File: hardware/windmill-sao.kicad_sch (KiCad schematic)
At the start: 27 parts, among them J1 SAO, J2 QWIIC, M1 SG90, U1 CH32V003F4P6

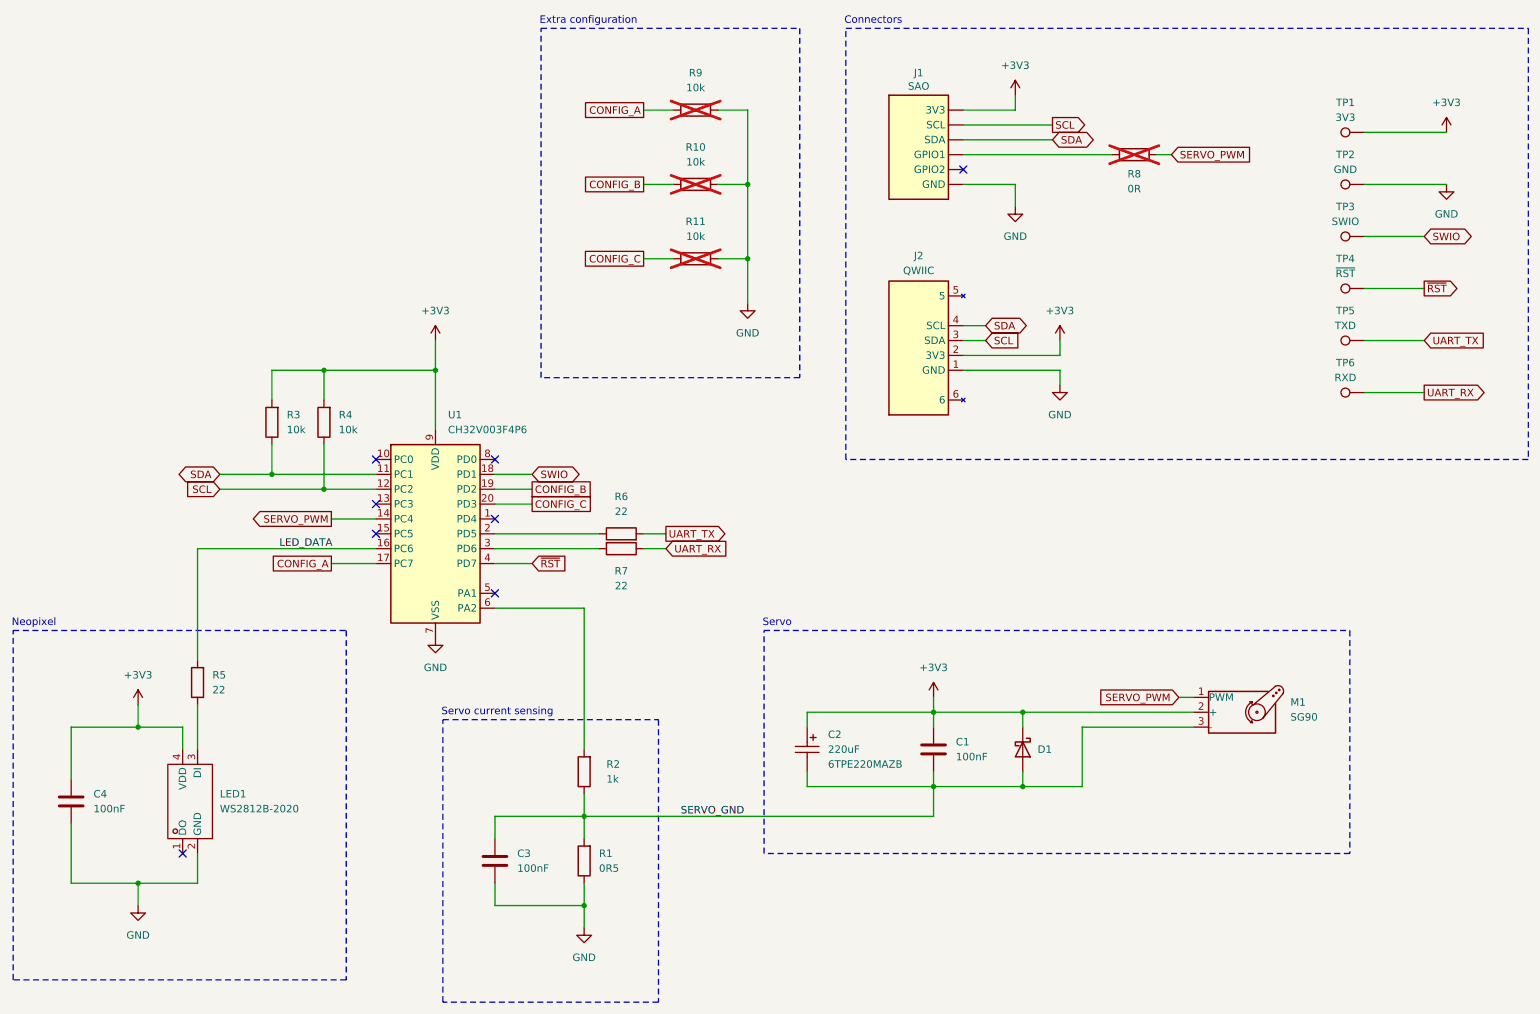
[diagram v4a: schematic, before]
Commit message: Add QWIIC logo and supplier part numbers
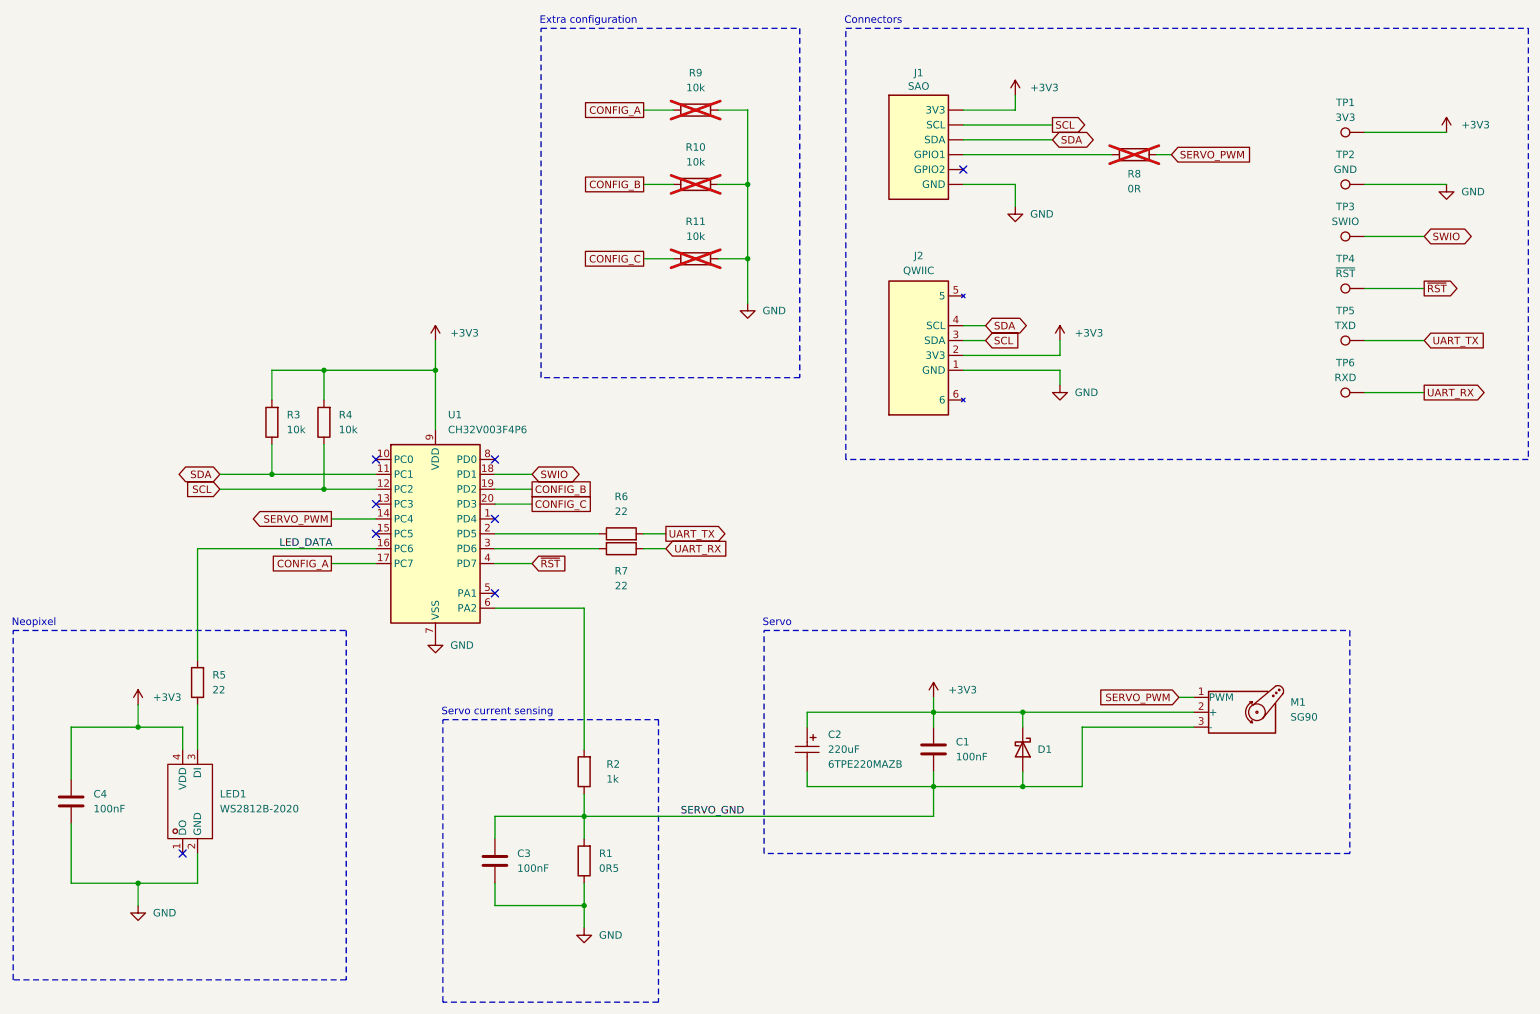
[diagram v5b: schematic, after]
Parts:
- C1, C3, C4: LCSC Part # (none) -> C14663
- C2: LCSC Part # (none) -> C79111; Supplier Part C79111 -> (none)
- D1: LCSC Part # (none) -> C2480
- J2: LCSC Part # (none) -> C160404; Supplier Part C160404 -> (none)
- LED1: JLCPCB Part # (none) -> C965555; LCSC Part # (none) -> C965555; Supplier Part C965555 -> (none)
- R1: LCSC Part # (none) -> C25340
- R2: LCSC Part # (none) -> C21190
- R3, R4: LCSC Part # (none) -> C25804
- R5, R6, R7: LCSC Part # (none) -> C23345
- U1: LCSC Part # (none) -> C5187096; Supplier Part C5187096 -> (none)
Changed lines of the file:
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@@
 			)
 		)
+		(property "LCSC Part #" "C21190"
+			(at 115.57 147.32 0)
+			(hide yes)
+			(show_name no)
+			(do_not_autoplace no)
+			(effects
+				(font
+					(size 1.27 1.27)
+				)
+			)
+		)
 		(pin "2"
 		)
@@
 		)
 		(property "Value" "+3V3"
-			(at 90.17 68.58 0)
+			(at 92.71 72.3899 0)
 			(show_name no)
 			(do_not_autoplace no)
@@
 					(size 1.27 1.27)
 				)
+				(justify left)
 			)
 		)
@@
 		(in_bom no)
 		(on_board yes)
-		(in_pos_files yes)
+		(in_pos_files no)
 		(dnp no)
 		(fields_autoplaced yes)
@@
 			)
 		)
-		(property "Supplier Part" "C79111"
+		(property "Supplier" "LCSC"
 			(at 153.67 143.51 0)
 			(hide yes)
@@
 			)
 		)
-		(property "Supplier" "LCSC"
+		(property "LCSC Part Name" "220uF ±20% 6.3V MSL=3拆包后请尽快使用"
 			(at 153.67 143.51 0)
 			(hide yes)
@@
 			)
 		)
-		(property "LCSC Part Name" "220uF ±20% 6.3V MSL=3拆包后请尽快使用"
+		(property "LCSC Part #" "C79111"
 			(at 153.67 143.51 0)
 			(hide yes)
@@
 		(in_bom no)
 		(on_board yes)
-		(in_pos_files yes)
+		(in_pos_files no)
 		(dnp no)
 		(fields_autoplaced yes)
@@
 		(in_bom no)
 		(on_board yes)
-		(in_pos_files yes)
+		(in_pos_files no)
 		(dnp no)
 		(fields_autoplaced yes)
@@
 			)
 		)
+		(property "LCSC Part #" "C23345"
+			(at 121.92 106.68 90)
+			(hide yes)
+			(show_name no)
+			(do_not_autoplace no)
+			(effects
+				(font
+					(size 1.27 1.27)
+				)
+			)
+		)
 		(pin "2"
 		)
@@
 		)
 		(property "Value" "GND"
-			(at 115.57 179.07 0)
+			(at 118.11 175.2599 0)
 			(show_name no)
 			(do_not_autoplace no)
@@
 					(size 1.27 1.27)
 				)
+				(justify left)
 			)
 		)
@@
 		)
 		(property "Value" "GND"
-			(at 189.23 55.88 0)
+			(at 191.77 52.0699 0)
 			(show_name no)
 			(do_not_autoplace no)
@@
 					(size 1.27 1.27)
 				)
+				(justify left)
 			)
 		)
@@
 		)
 		(property "Value" "GND"
-			(at 196.85 86.36 0)
+			(at 199.39 82.5499 0)
 			(show_name no)
 			(do_not_autoplace no)
@@
 					(size 1.27 1.27)
 				)
+				(justify left)
 			)
 		)
@@
 			)
 		)
+		(property "LCSC Part #" "C14663"
+			(at 175.26 143.51 0)
+			(hide yes)
+			(show_name no)
+			(do_not_autoplace no)
+			(effects
+				(font
+					(size 1.27 1.27)
+				)
+			)
+		)
 		(pin "1"
 		)
@@
 		)
 		(property "Value" "+3V3"
-			(at 196.85 68.58 0)
+			(at 199.39 72.3899 0)
 			(show_name no)
 			(do_not_autoplace no)
@@
 					(size 1.27 1.27)
 				)
+				(justify left)
 			)
 		)
@@
 			)
 		)
-		(property "Supplier Part" "C5187096"
+		(property "LCSC Part #" "C5187096"
 			(at 90.17 106.68 0)
 			(hide yes)
@@
 		)
 		(property "Value" "+3V3"
-			(at 262.89 33.02 0)
+			(at 265.43 36.8299 0)
 			(show_name no)
 			(do_not_autoplace no)
@@
 					(size 1.27 1.27)
 				)
+				(justify left)
 			)
 		)
@@
 			)
 		)
+		(property "LCSC Part #" "C25340"
+			(at 115.57 162.56 0)
+			(hide yes)
+			(show_name no)
+			(do_not_autoplace no)
+			(effects
+				(font
+					(size 1.27 1.27)
+				)
+			)
+		)
 		(pin "2"
 		)
@@
 		(in_bom no)
 		(on_board yes)
-		(in_pos_files yes)
+		(in_pos_files no)
 		(dnp no)
 		(fields_autoplaced yes)
@@
 			)
 		)
+		(property "LCSC Part #" "C14663"
+			(at 100.33 162.56 0)
+			(hide yes)
+			(show_name no)
+			(do_not_autoplace no)
+			(effects
+				(font
+					(size 1.27 1.27)
+				)
+			)
+		)
 		(pin "1"
 		)
@@
 		)
 		(property "Value" "+3V3"
-			(at 189.23 26.67 0)
+			(at 191.77 30.4799 0)
 			(show_name no)
 			(do_not_autoplace no)
@@
 					(size 1.27 1.27)
 				)
+				(justify left)
 			)
 		)
@@
 			)
 		)
-		(property "Supplier Part" "C965555"
+		(property "JLCPCB Part #" "C965555"
 			(at 48.26 152.4 0)
 			(hide yes)
@@
 			)
 		)
+		(property "LCSC Part #" "C965555"
+			(at 48.26 152.4 0)
+			(hide yes)
+			(show_name no)
+			(do_not_autoplace no)
+			(effects
+				(font
+					(size 1.27 1.27)
+				)
+			)
+		)
 		(pin "4"
 		)
@@
 		)
 		(property "Value" "GND"
-			(at 90.17 129.54 0)
+			(at 92.71 125.7299 0)
 			(show_name no)
 			(do_not_autoplace no)
@@
 					(size 1.27 1.27)
 				)
+				(justify left)
 			)
 		)
@@
 			)
 		)
-		(property "Supplier Part" "C160404"
+		(property "LCSC Part #" "C160404"
 			(at 176.53 74.93 90)
 			(hide yes)
@@
 		(in_bom no)
 		(on_board yes)
-		(in_pos_files yes)
+		(in_pos_files no)
 		(dnp no)
 		(fields_autoplaced yes)
@@
 		)
 		(property "Value" "GND"
-			(at 39.37 175.26 0)
+			(at 41.91 171.4499 0)
 			(show_name no)
 			(do_not_autoplace no)
@@
 					(size 1.27 1.27)
 				)
+				(justify left)
 			)
 		)
@@
 			)
 		)
+		(property "LCSC Part #" "C23345"
+			(at 49.53 132.08 0)
+			(hide yes)
+			(show_name no)
+			(do_not_autoplace no)
+			(effects
+				(font
+					(size 1.27 1.27)
+				)
+			)
+		)
 		(pin "2"
 		)
@@
 			)
 		)
+		(property "LCSC Part #" "C23345"
+			(at 121.92 109.22 90)
+			(hide yes)
+			(show_name no)
+			(do_not_autoplace no)
+			(effects
+				(font
+					(size 1.27 1.27)
+				)
+			)
+		)
 		(pin "2"
 		)
@@
 			)
 		)
+		(property "LCSC Part #" "C25804"
+			(at 62.23 87.63 0)
+			(hide yes)
+			(show_name no)
+			(do_not_autoplace no)
+			(effects
+				(font
+					(size 1.27 1.27)
+				)
+			)
+		)
 		(pin "2"
 		)
@@
 			)
 		)
+		(property "LCSC Part #" "C25804"
+			(at 71.12 87.63 0)
+			(hide yes)
+			(show_name no)
+			(do_not_autoplace no)
+			(effects
+				(font
+					(size 1.27 1.27)
+				)
+			)
+		)
 		(pin "2"
 		)
@@
 			)
 		)
+		(property "LCSC Part #" "C2480"
+			(at 190.5 143.51 90)
+			(hide yes)
+			(show_name no)
+			(do_not_autoplace no)
+			(effects
+				(font
+					(size 1.27 1.27)
+				)
+			)
+		)
 		(pin "2"
 		)
@@
 		)
 		(property "Value" "GND"
-			(at 262.89 52.07 0)
+			(at 265.43 48.2599 0)
 			(show_name no)
 			(do_not_autoplace no)
@@
 					(size 1.27 1.27)
 				)
+				(justify left)
 			)
 		)
@@
 		)
 		(property "Value" "+3V3"
-			(at 175.26 129.54 0)
+			(at 177.8 133.3499 0)
 			(show_name no)
 			(do_not_autoplace no)
@@
 					(size 1.27 1.27)
 				)
+				(justify left)
 			)
 		)
@@
 		)
 		(property "Value" "+3V3"
-			(at 39.37 130.81 0)
+			(at 41.91 134.6199 0)
 			(show_name no)
 			(do_not_autoplace no)
@@
 					(size 1.27 1.27)
 				)
+				(justify left)
 			)
 		)
@@
 			)
 		)
+		(property "LCSC Part #" "C14663"
+			(at 27.94 152.4 0)
+			(hide yes)
+			(show_name no)
+			(do_not_autoplace no)
+			(effects
+				(font
+					(size 1.27 1.27)
+				)
+			)
+		)
 		(pin "1"
 		)
@@
 		)
 		(property "Value" "GND"
-			(at 143.51 72.39 0)
+			(at 146.05 68.5799 0)
 			(show_name no)
 			(do_not_autoplace no)
@@
 					(size 1.27 1.27)
 				)
+				(justify left)
 			)
 		)
@@
 		(in_bom no)
 		(on_board yes)
-		(in_pos_files yes)
+		(in_pos_files no)
 		(dnp no)
 		(fields_autoplaced yes)

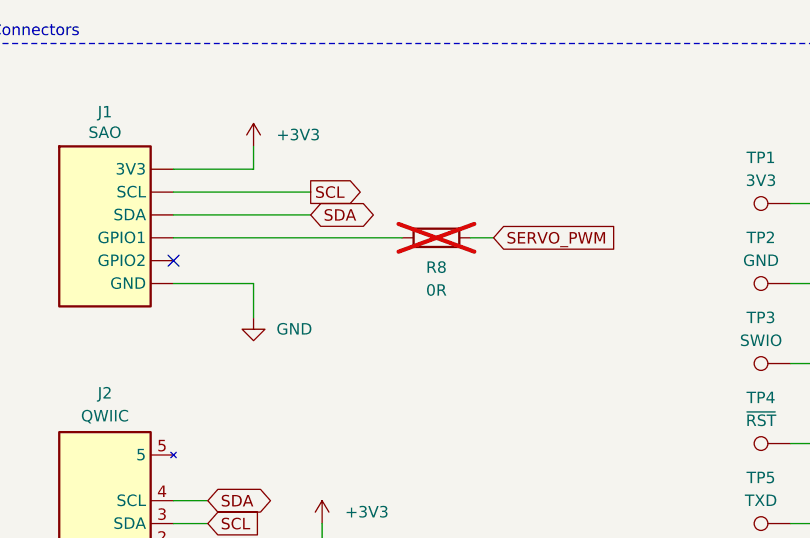
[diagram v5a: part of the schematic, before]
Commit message: Add C5 and clean up silkscreen even more
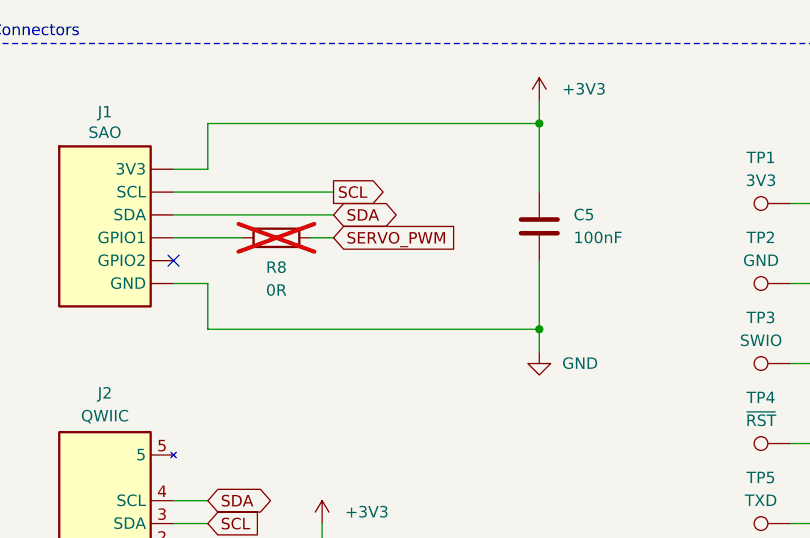
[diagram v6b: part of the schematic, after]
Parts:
- added C5: 100nF, Capacitor_SMD:C_0603_1608Metric_Pad1.08x0.95mm_HandSolder, symbol Device:C
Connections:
- net +3V3: now also C5.1
- net GND: now also C5.2
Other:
- moved on the sheet: R8
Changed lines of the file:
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@@
 	)
 	(junction
+		(at 220.98 29.21)
+		(diameter 0)
+		(color 0 0 0 0)
+	)
+	(junction
 		(at 143.51 59.69)
 		(diameter 0)
@@
 		(color 0 0 0 0)
 	)
+	(junction
+		(at 220.98 52.07)
+		(diameter 0)
+		(color 0 0 0 0)
+	)
 	(no_connect
 		(at 80.01 106.68)
@@
 	(wire
 		(pts
+			(xy 220.98 52.07) (xy 184.15 52.07)
+		)
+		(stroke
+			(width 0)
+			(type default)
+		)
+	)
+	(wire
+		(pts
 			(xy 180.34 73.66) (xy 184.15 73.66)
 		)
@@
 	(wire
 		(pts
-			(xy 189.23 31.75) (xy 189.23 34.29)
+			(xy 220.98 26.67) (xy 220.98 29.21)
 		)
 		(stroke
@@
 	(wire
 		(pts
-			(xy 180.34 46.99) (xy 189.23 46.99)
+			(xy 180.34 46.99) (xy 184.15 46.99)
 		)
 		(stroke
@@
 	(wire
 		(pts
-			(xy 180.34 39.37) (xy 195.58 39.37)
+			(xy 220.98 44.45) (xy 220.98 52.07)
+		)
+		(stroke
+			(width 0)
+			(type default)
+		)
+	)
+	(wire
+		(pts
+			(xy 180.34 39.37) (xy 198.12 39.37)
 		)
 		(stroke
@@
 	(wire
 		(pts
+			(xy 184.15 29.21) (xy 184.15 34.29)
+		)
+		(stroke
+			(width 0)
+			(type default)
+		)
+	)
+	(wire
+		(pts
 			(xy 125.73 46.99) (xy 130.81 46.99)
 		)
@@
 	(wire
 		(pts
+			(xy 184.15 29.21) (xy 220.98 29.21)
+		)
+		(stroke
+			(width 0)
+			(type default)
+		)
+	)
+	(wire
+		(pts
 			(xy 248.92 55.88) (xy 259.08 55.88)
 		)
@@
 	(wire
 		(pts
-			(xy 180.34 36.83) (xy 195.58 36.83)
+			(xy 180.34 36.83) (xy 198.12 36.83)
 		)
 		(stroke
@@
 	(wire
 		(pts
-			(xy 189.23 46.99) (xy 189.23 50.8)
+			(xy 184.15 46.99) (xy 184.15 52.07)
 		)
 		(stroke
@@
 	(wire
 		(pts
-			(xy 180.34 34.29) (xy 189.23 34.29)
+			(xy 180.34 34.29) (xy 184.15 34.29)
 		)
 		(stroke
@@
 	(wire
 		(pts
-			(xy 180.34 41.91) (xy 205.74 41.91)
+			(xy 180.34 41.91) (xy 187.96 41.91)
 		)
 		(stroke
@@
 	(wire
 		(pts
-			(xy 213.36 41.91) (xy 215.9 41.91)
+			(xy 195.58 41.91) (xy 198.12 41.91)
 		)
 		(stroke
@@
 	(wire
 		(pts
+			(xy 220.98 29.21) (xy 220.98 36.83)
+		)
+		(stroke
+			(width 0)
+			(type default)
+		)
+	)
+	(wire
+		(pts
 			(xy 180.34 78.74) (xy 196.85 78.74)
 		)
@@
 	(wire
 		(pts
+			(xy 220.98 52.07) (xy 220.98 54.61)
+		)
+		(stroke
+			(width 0)
+			(type default)
+		)
+	)
+	(wire
+		(pts
 			(xy 200.66 139.7) (xy 219.71 139.7)
 		)
@@
 	(global_label "SCL"
 		(shape output)
-		(at 195.58 36.83 0)
+		(at 198.12 36.83 0)
 		(fields_autoplaced yes)
 		(effects
@@
 		)
 		(property "Intersheetrefs" "${INTERSHEET_REFS}"
-			(at 202.0728 36.83 0)
+			(at 204.6128 36.83 0)
 			(hide yes)
 			(show_name no)
@@
 	(global_label "SERVO_PWM"
 		(shape input)
-		(at 215.9 41.91 0)
+		(at 198.12 41.91 0)
 		(fields_autoplaced yes)
 		(effects
@@
 		)
 		(property "Intersheetrefs" "${INTERSHEET_REFS}"
-			(at 230.0732 41.91 0)
+			(at 212.2932 41.91 0)
 			(hide yes)
 			(show_name no)
@@
 	(global_label "SDA"
 		(shape bidirectional)
-		(at 195.58 39.37 0)
+		(at 198.12 39.37 0)
 		(fields_autoplaced yes)
 		(effects
@@
 		)
 		(property "Intersheetrefs" "${INTERSHEET_REFS}"
-			(at 203.2446 39.37 0)
+			(at 205.7846 39.37 0)
 			(hide yes)
 			(show_name no)
@@
 	(symbol
 		(lib_id "power:GND")
-		(at 189.23 50.8 0)
+		(at 220.98 54.61 0)
 		(unit 1)
 		(body_style 1)
@@
 		(fields_autoplaced yes)
 		(property "Reference" "#PWR01"
-			(at 189.23 57.15 0)
+			(at 220.98 60.96 0)
 			(hide yes)
 			(show_name no)
@@
 		)
 		(property "Value" "GND"
-			(at 191.77 52.0699 0)
+			(at 223.52 55.8799 0)
 			(show_name no)
 			(do_not_autoplace no)
@@
 		)
 		(property "Footprint" ""
-			(at 189.23 50.8 0)
+			(at 220.98 54.61 0)
 			(hide yes)
 			(show_name no)
@@
 		)
 		(property "Datasheet" ""
-			(at 189.23 50.8 0)
+			(at 220.98 54.61 0)
 			(hide yes)
 			(show_name no)
@@
 		)
 		(property "Description" "Power symbol creates a global label with name \"GND\" , ground"
-			(at 189.23 50.8 0)
+			(at 220.98 54.61 0)
 			(hide yes)
 			(show_name no)
@@
 	(symbol
 		(lib_id "Device:R")
-		(at 209.55 41.91 90)
+		(at 191.77 41.91 90)
 		(mirror x)
 		(unit 1)
@@
 		(dnp yes)
 		(property "Reference" "R8"
-			(at 209.55 45.212 90)
+			(at 191.77 45.212 90)
 			(show_name no)
 			(do_not_autoplace no)
@@
 		)
 		(property "Value" "0R"
-			(at 209.55 47.752 90)
+			(at 191.77 47.752 90)
 			(show_name no)
 			(do_not_autoplace no)
@@
 		)
 		(property "Footprint" "Resistor_SMD:R_0603_1608Metric_Pad0.98x0.95mm_HandSolder"
-			(at 209.55 40.132 90)
+			(at 191.77 40.132 90)
 			(hide yes)
 			(show_name no)
@@
 		)
 		(property "Datasheet" ""
-			(at 209.55 41.91 0)
+			(at 191.77 41.91 0)
 			(hide yes)
 			(show_name no)
@@
 		)
 		(property "Description" "Resistor"
-			(at 209.55 41.91 0)
+			(at 191.77 41.91 0)
 			(hide yes)
 			(show_name no)
@@
 	(symbol
 		(lib_id "power:+3V3")
-		(at 189.23 31.75 0)
+		(at 220.98 26.67 0)
 		(unit 1)
 		(body_style 1)
@@
 		(fields_autoplaced yes)
 		(property "Reference" "#PWR02"
-			(at 189.23 35.56 0)
+			(at 220.98 30.48 0)
 			(hide yes)
 			(show_name no)
@@
 		)
 		(property "Value" "+3V3"
-			(at 191.77 30.4799 0)
+			(at 223.52 25.3999 0)
 			(show_name no)
 			(do_not_autoplace no)
@@
 		)
 		(property "Footprint" ""
-			(at 189.23 31.75 0)
+			(at 220.98 26.67 0)
 			(hide yes)
 			(show_name no)
@@
 		)
 		(property "Datasheet" ""
-			(at 189.23 31.75 0)
+			(at 220.98 26.67 0)
 			(hide yes)
 			(show_name no)
@@
 		)
 		(property "Description" "Power symbol creates a global label with name \"+3V3\""
-			(at 189.23 31.75 0)
+			(at 220.98 26.67 0)
 			(hide yes)
 			(show_name no)
@@
 					(unit 1)
 				)
+			)
+		)
+	)
+	(symbol
+		(lib_id "Device:C")
+		(at 220.98 40.64 0)
+		(unit 1)
+		(body_style 1)
+		(exclude_from_sim no)
+		(in_bom yes)
+		(on_board yes)
+		(in_pos_files yes)
+		(dnp no)
+		(fields_autoplaced yes)
+		(property "Reference" "C5"
+			(at 224.79 39.3699 0)
+			(show_name no)
+			(do_not_autoplace no)
+			(effects
+				(font
+					(size 1.27 1.27)
+				)
+				(justify left)
+			)
+		)
+		(property "Value" "100nF"
+			(at 224.79 41.9099 0)
+			(show_name no)
+			(do_not_autoplace no)
+			(effects
+				(font
+					(size 1.27 1.27)
+				)
+				(justify left)
+			)
+		)
+		(property "Footprint" "Capacitor_SMD:C_0603_1608Metric_Pad1.08x0.95mm_HandSolder"
+			(at 221.9452 44.45 0)
+			(hide yes)
+			(show_name no)
+			(do_not_autoplace no)
+			(effects
+				(font
+					(size 1.27 1.27)
+				)
+			)
+		)
+		(property "Datasheet" ""
+			(at 220.98 40.64 0)
+			(hide yes)
+			(show_name no)
+			(do_not_autoplace no)
+			(effects
+				(font
+					(size 1.27 1.27)
+				)
+			)
+		)
+		(property "Description" "Unpolarized capacitor"
+			(at 220.98 40.64 0)
+			(hide yes)
+			(show_name no)
+			(do_not_autoplace no)
+			(effects
+				(font
+					(size 1.27 1.27)
+				)
+			)
+		)
+		(property "LCSC Part #" "C14663"
+			(at 220.98 40.64 0)
+			(hide yes)
+			(show_name no)
+			(do_not_autoplace no)
+			(effects
+				(font
+					(size 1.27 1.27)
+				)
+			)
+		)
+		(pin "1"
+		)
+		(pin "2"
+		)
+		(instances
+			(project "windmill-sao"
+				(path "/8df7e88c-ef31-4b76-9151-6aa024d57978"
+					(reference "C5")
+					(unit 1)
+				)
